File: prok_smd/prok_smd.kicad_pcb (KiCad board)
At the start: 2 copper layers, 105 x 39.5 mm, 54 parts, among them CON1 microSD_Card, J1 POWER, J10 Conn_01x04_Female, J11 Conn_01x04_Female, J12 Conn_01x05_Male, J13 Conn_01x04_Male, J14 Conn_01x04_Male, J2 EXPAND, J5 TIME_CV, J6 CHANNEL_CV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

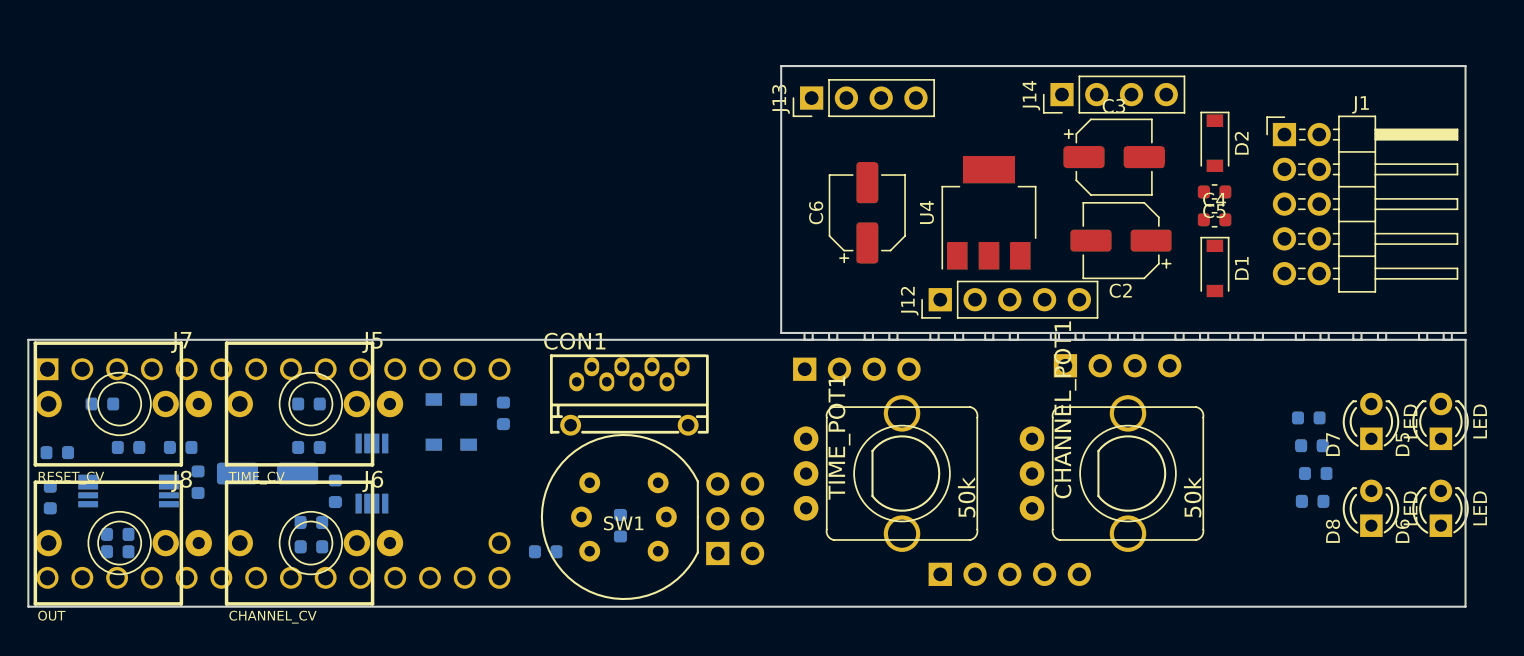
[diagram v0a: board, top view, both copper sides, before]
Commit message: :construction: Aligned UI elements to panel specs
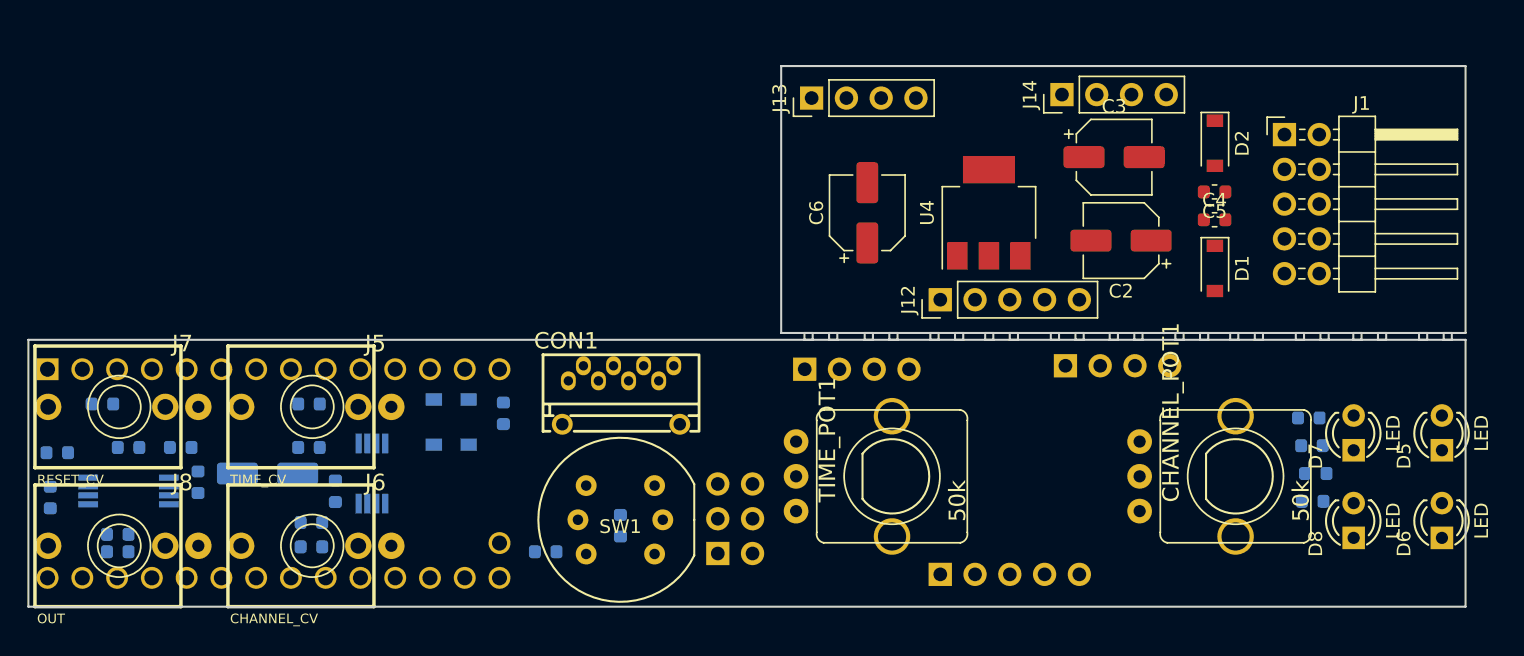
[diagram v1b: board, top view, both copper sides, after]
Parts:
- moved CHANNEL_POT1 7.86 mm to (188.2, 65.0)
- moved D8 1.57 mm to (196.8, 68.2)
- moved D7 1.54 mm to (196.8, 61.8)
- moved D6 0.89 mm to (203.3, 68.2)
- moved D5 0.84 mm to (203.3, 61.8)
- moved TIME_POT1 0.76 mm to (163.1, 65.0)
- moved CON1 0.61 mm to (142.9, 59.6)
- moved SW1 0.33 mm to (143.2, 68.2)
- moved J5 0.23 mm to (120.8, 59.9)
- moved J6 0.22 mm to (120.8, 70.0)
- moved J7 0.21 mm to (106.7, 59.9)
- moved J8 0.20 mm to (106.7, 70.0)

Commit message: :construction: Locked headers and added mousebites
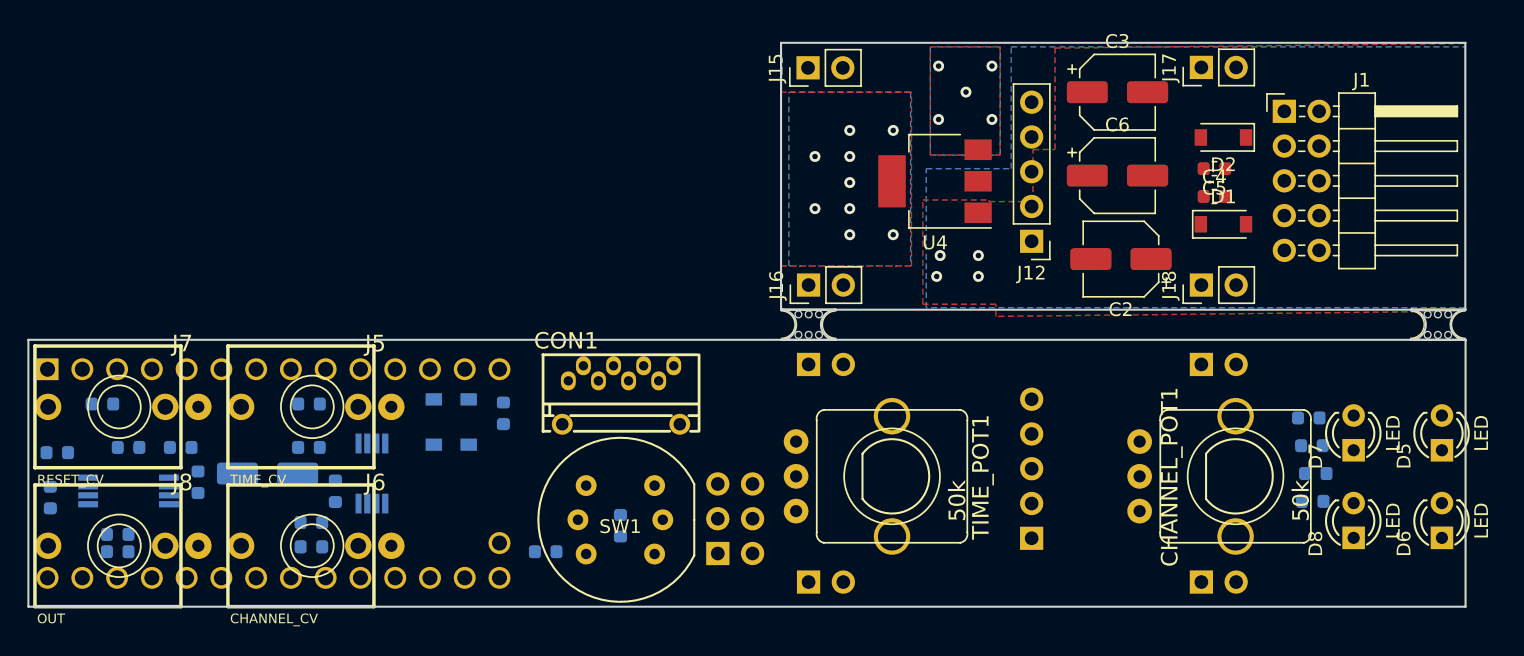
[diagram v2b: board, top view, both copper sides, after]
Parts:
- added J15: Conn_01x02_Male, Connector_PinHeader_2.54mm:PinHeader_1x02_P2.54mm_Vertical, F.Cu at (157.0, 35.1)
- added J16: Conn_01x02_Male, Connector_PinHeader_2.54mm:PinHeader_1x02_P2.54mm_Vertical, F.Cu at (157.0, 51.0)
- added J17: Conn_01x02_Male, Connector_PinHeader_2.54mm:PinHeader_1x02_P2.54mm_Vertical, F.Cu at (185.7, 35.1)
- added J18: Conn_01x02_Male, Connector_PinHeader_2.54mm:PinHeader_1x02_P2.54mm_Vertical, F.Cu at (185.7, 51.0)
- added mouse-bite-2mm-slot: VAL**, Panelization:mouse-bite-2mm-slot, F.Cu at (157.0, 53.9)
- added mouse-bite-2mm-slot: VAL**, Panelization:mouse-bite-2mm-slot, F.Cu at (203.0, 53.9)
- J10, J11: value Conn_01x04_Female -> Conn_01x02_Female; footprint Connector_PinSocket_2.54mm:PinSocket_1x04_P2.54mm_Vertical -> Connector_PinSocket_2.54mm:PinSocket_1x02_P2.54mm_Vertical
- J13, J14: value Conn_01x04_Male -> Conn_01x02_Female; footprint Connector_PinHeader_2.54mm:PinHeader_1x04_P2.54mm_Vertical -> Connector_PinSocket_2.54mm:PinSocket_1x02_P2.54mm_Vertical; moved to B.Cu
- moved J13 45.4 mm to (185.7, 72.7), turned to 270 degrees
- moved J14 40.1 mm to (157.0, 72.7), turned to 270 degrees
- moved C6 18.5 mm to (179.6, 43.0), turned to 0 degrees
- moved J11 9.93 mm to (185.7, 56.8)
- moved J12 7.92 mm to (173.3, 47.8), turned to 180 degrees
- moved J9 7.18 mm to (173.3, 69.5), turned to 0 degrees
- moved C3 4.75 mm to (179.6, 36.9)
- moved U4 4.56 mm to (166.2, 43.4), turned to 180 degrees
- moved D1 3.28 mm to (187.3, 46.6), turned to 0 degrees
- moved C4 1.70 mm to (186.7, 44.5)
- moved J1 1.70 mm to (191.8, 38.3)
- moved C5 1.70 mm to (186.7, 42.5)
- moved C2 1.35 mm to (179.8, 49.1)
- moved D2 0.76 mm to (187.3, 40.2), turned to 180 degrees
- moved J10 0.45 mm to (157.0, 56.8)
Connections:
- J10 pad 1: GND -> Net-(J10-Pad1)
- J10 pad 2: Net-(J10-Pad2) -> GND
- J11 pad 2: Net-(J10-Pad3) -> Net-(J11-Pad2)
- J12 pad 3: -12V -> +5V
- J12 pad 5: +5V -> -12V
- J13 pad 2: Net-(J13-Pad2) -> Net-(J10-Pad1)
- J14 pad 1: GND -> Net-(J11-Pad2)
- J14 pad 2: Net-(J13-Pad3) -> GND
- J9 pad 3: -12V -> +5V
- J9 pad 5: +5V -> -12V
- U4 pad 4: (no net) -> Net-(HS1-Pad1)
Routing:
- net Net-(HS1-Pad1): vias 0 -> 9
- net GND: vias 0 -> 4
- net +12V: vias 0 -> 5
- added copper zone on B.Cu, net +12V
- added copper zone on F.Cu, net +12V
- added copper zone on B.Cu, net GND
- added copper zone on F.Cu, net GND
- added copper zone on B.Cu, net Net-(HS1-Pad1)
- added copper zone on F.Cu, net Net-(HS1-Pad1)
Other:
- board size 105 x 39.5 mm -> 105 x 41.2 mm

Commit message: :construction: first draft routing
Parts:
- moved R13 13.1 mm to (203.2, 57.7), turned to 270 degrees
- moved R16 12.1 mm to (196.8, 72.4), turned to 90 degrees
- moved R14 11.9 mm to (203.2, 72.4), turned to 90 degrees
- moved R15 5.92 mm to (196.8, 57.7), turned to 270 degrees
- turned D6 to 90 degrees
- turned D8 to 90 degrees
- turned R18 to 270 degrees
- turned R6 to 180 degrees
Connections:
- J10 pad 1: Net-(J10-Pad1) -> GND
- J11 pad 2: Net-(J11-Pad2) -> GND
- J13 pad 2: Net-(J10-Pad1) -> GND
- J14 pad 1: Net-(J11-Pad2) -> GND
- J15 pad 2: Net-(J15-Pad2) -> GND
- J16 pad 1: Net-(J16-Pad1) -> GND
- J17 pad 1: Net-(J15-Pad2) -> GND
- J18 pad 2: Net-(J16-Pad1) -> GND
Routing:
- net LED_1: track 0.00 -> 100.3 mm, vias 0 -> 1
- net LED_2: track 0.00 -> 100.1 mm, vias 0 -> 1
- net +12V: track 0.00 -> 98.7 mm, vias 5 -> 7
- net LED_4: track 0.00 -> 91.5 mm, vias 0 -> 1
- net +5V: track 0.00 -> 91.2 mm, vias 0 -> 1
- net LED_3: track 0.00 -> 88.8 mm, vias 0 -> 1
- net -12V: track 0.00 -> 88.6 mm, vias 0 -> 3
- net +3V3: track 0.00 -> 87.1 mm, vias 0 -> 3
- net CHANNEL_POT: track 0.00 -> 79.7 mm, vias 0 -> 2
- net TIME_POT: track 0.00 -> 50.0 mm, vias 0 -> 6
- net RESET_SW: track 0.00 -> 35.6 mm
- net A4: track 0.00 -> 35.2 mm
- net A5: track 0.00 -> 35.0 mm
- net RESET_CV: track 0.00 -> 33.0 mm, vias 0 -> 1
- net GND: track 0.00 -> 29.4 mm
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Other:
- net class Default: clearance 0.2 -> 0.127; trace_width 0.25 -> 0.127; via_dia 0.8 -> 0.6; via_drill 0.4 -> 0.3
- rule trace_clearance: 0.2 -> 0.127
- rule trace_min: 0.2 -> 0.127
- rule via_min_size: 0.4 -> 0.6

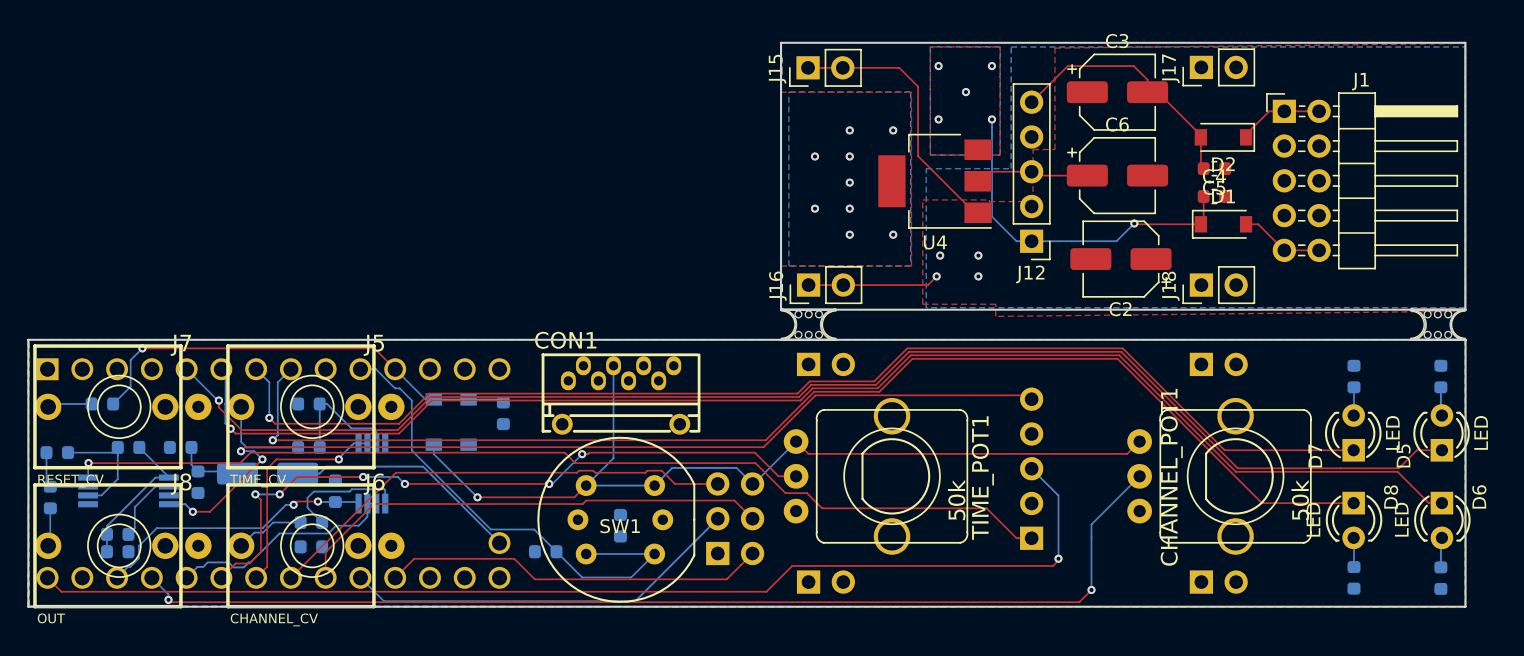
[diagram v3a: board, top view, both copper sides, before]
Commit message: :sparkles: finished first draft routing. Matched lengths for SD card traces
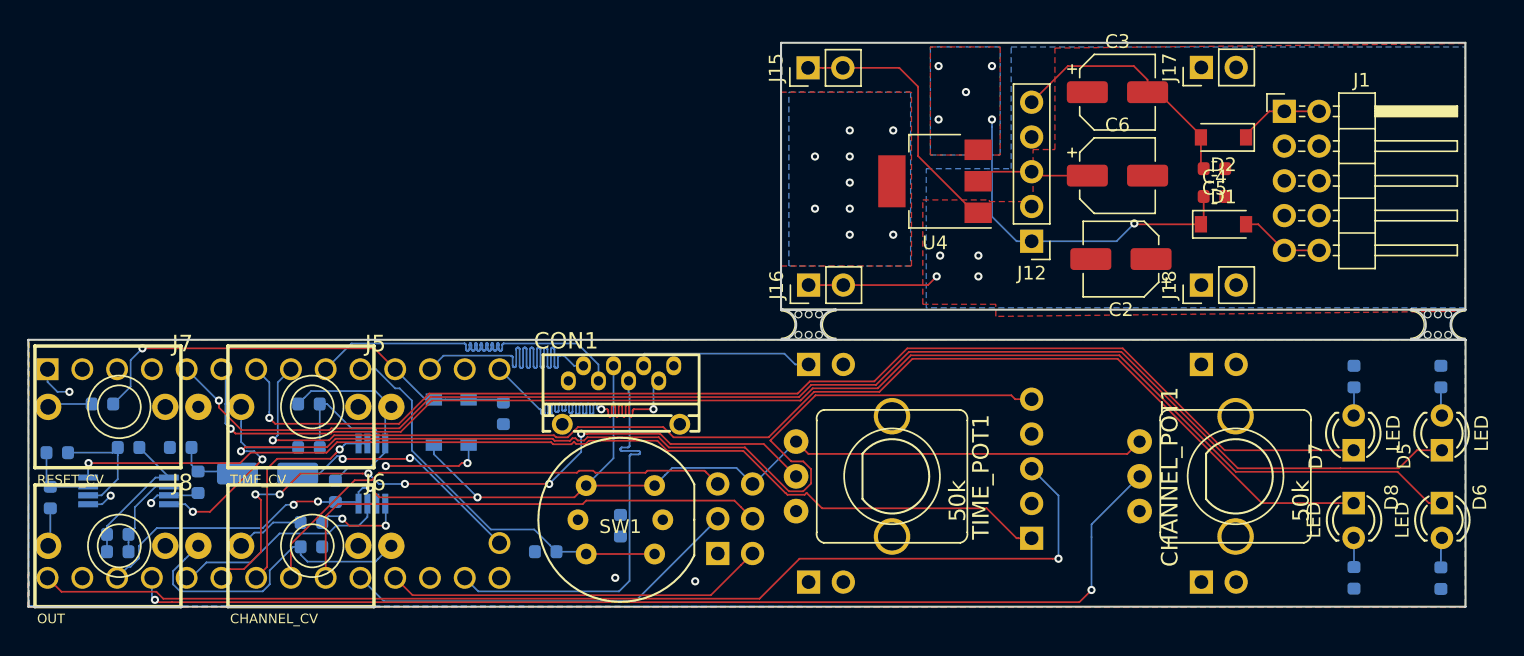
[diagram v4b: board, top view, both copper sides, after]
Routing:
- net GND: track 29.4 -> 97.2 mm, vias 4 -> 11
- net MISO: track 0.00 -> 30.0 mm, vias 0 -> 2
- net SS: track 0.00 -> 30.0 mm
- net SCLK: track 0.00 -> 30.0 mm
- net MOSI: track 0.00 -> 29.8 mm
- net -12V: track 88.6 -> 98.7 mm
- net +3V3: track 87.1 -> 97.1 mm, vias 3 -> 4
- net RESET_SW: track 35.6 -> 29.2 mm
- net CHANNEL_CV: track 9.18 -> 6.75 mm, vias 0 -> 2
- net TIME_POT: track 50.0 -> 52.1 mm
- net A4: track 35.2 -> 36.7 mm
- net A5: track 35.0 -> 36.4 mm
- net Net-(C8-Pad1): track 5.29 -> 6.56 mm
- net +12V: track 98.7 -> 99.8 mm
- net LED_4: track 91.5 -> 92.3 mm
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
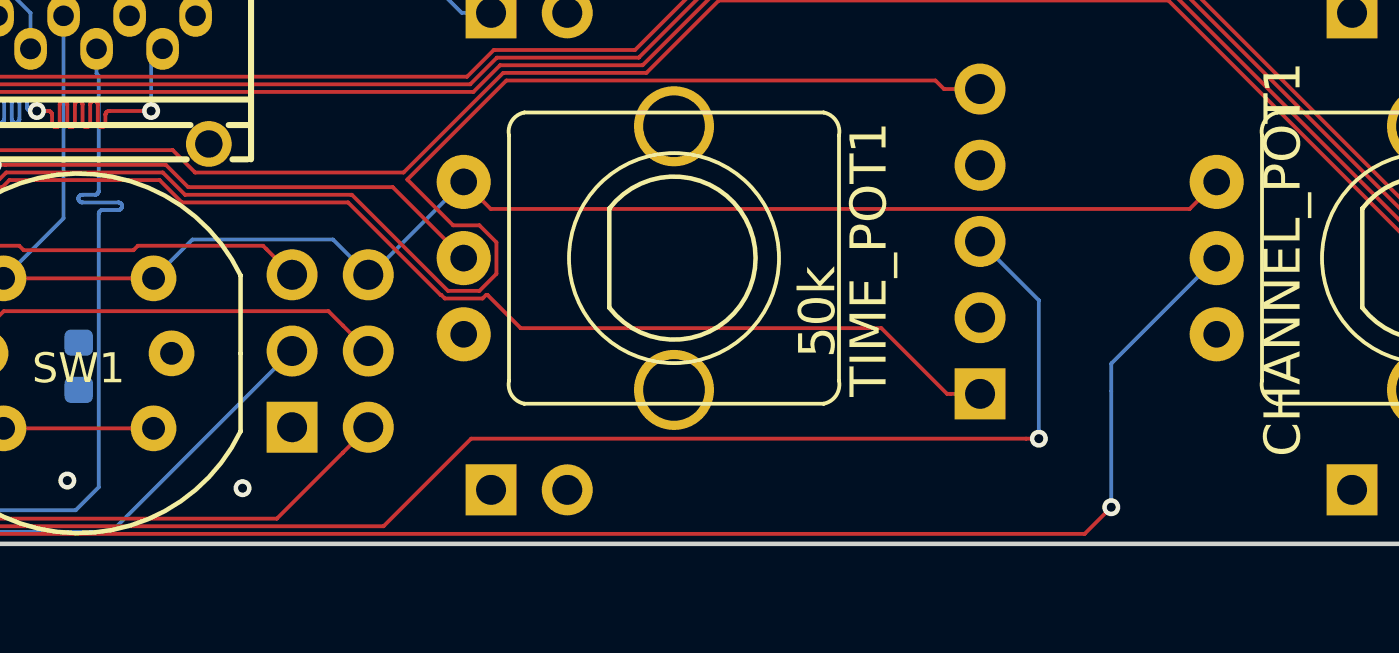
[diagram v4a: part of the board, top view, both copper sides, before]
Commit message: :bug: fixed backwards pots
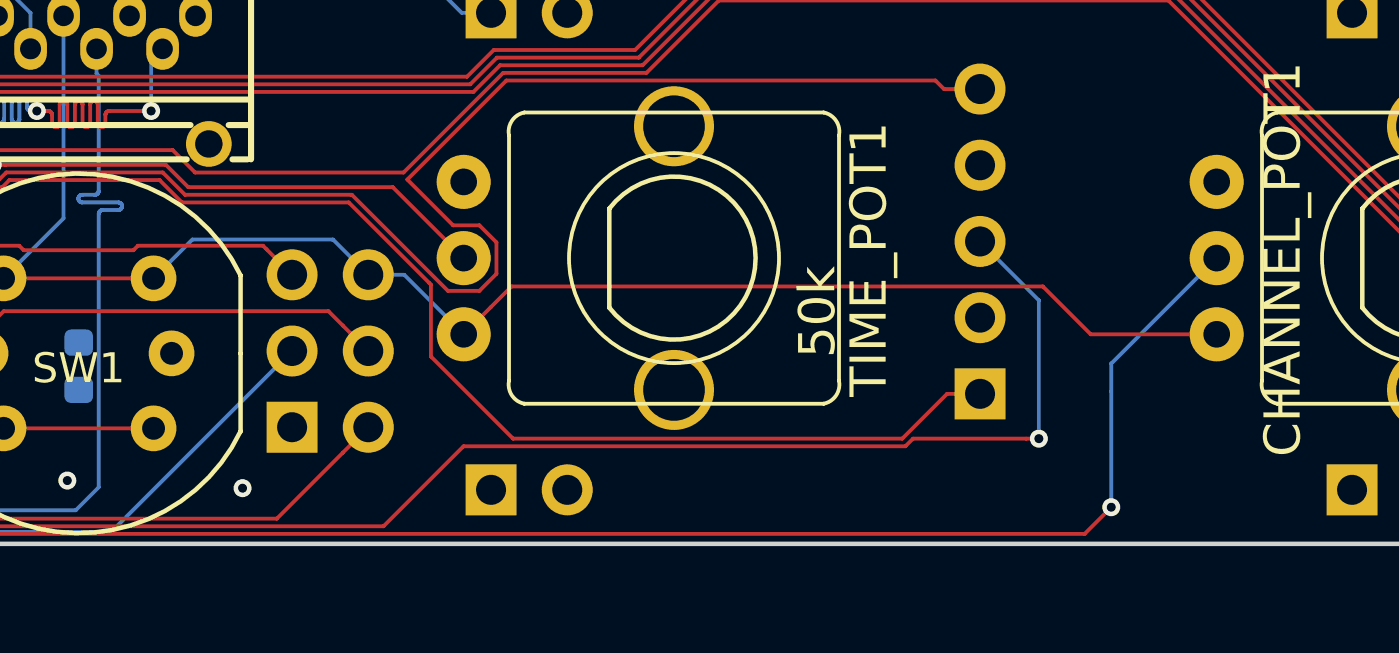
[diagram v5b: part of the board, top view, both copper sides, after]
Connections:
- CHANNEL_POT1 pad 1: +3V3 -> GND
- CHANNEL_POT1 pad 3: GND -> +3V3
- TIME_POT1 pad 1: +3V3 -> GND
- TIME_POT1 pad 3: GND -> +3V3
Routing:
- net +12V: track 99.8 -> 102.3 mm

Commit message: :sparkles: Fixed switch led
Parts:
- SW1: value KS01BL -> SW_Push_LED
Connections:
- R17 pad 2: Net-(D9-Pad1) -> Net-(R17-Pad2)
- SW1 pad 3: (no net) -> Net-(R17-Pad2)
- SW1 pad 4: (no net) -> LED_RESET
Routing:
- net LED_RESET: track 0.00 -> 15.9 mm
- net Net-(R17-Pad2): track 0.00 -> 6.29 mm, vias 0 -> 1
